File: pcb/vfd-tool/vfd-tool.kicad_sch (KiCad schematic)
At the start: 50 parts, among them J1 Micro_SD_Card, J2 Conn_02x03_Top_Bottom, J3 USB_C_Receptacle_USB2.0, SW1 SW_Push, SW2 SW_Push, U1 RP2040, U2 W25Q32JVSS, U3 TPS562200, Y1 Crystal_GND24

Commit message: Charging circuitry kinda done
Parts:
- added C21, C22: 10uF, Capacitor_SMD:C_0402_1005Metric_Pad0.74x0.62mm_HandSolder, symbol Device:C
- added C23, C26: 0.1uF, Capacitor_SMD:C_0402_1005Metric_Pad0.74x0.62mm_HandSolder, symbol Device:C
- added C24, C25: 22uF, Capacitor_SMD:C_0402_1005Metric_Pad0.74x0.62mm_HandSolder, symbol Device:C
- added C27: 10nF, Capacitor_SMD:C_0402_1005Metric_Pad0.74x0.62mm_HandSolder, symbol Device:C_Small
- added C28: 1uF, Capacitor_SMD:C_0603_1608Metric_Pad1.08x0.95mm_HandSolder, symbol Device:C
- added C29, C30: 4.7uF, Capacitor_SMD:C_0603_1608Metric_Pad1.08x0.95mm_HandSolder, symbol Device:C
- added C31: 0.1uF, Capacitor_SMD:C_0603_1608Metric, symbol Device:C
- added D10, D2: D_Schottky, symbol Device:D_Schottky
- added D3: WS2812B-2020, LED_SMD:LED_WS2812B-2020_PLCC4_2.0x2.0mm, symbol LED:WS2812B-2020
- added D4, D5: LED, LED_SMD:LED_0603_1608Metric, symbol Device:LED
- added D6: PMEG4010CEJ, Diode_SMD:D_SOD-323_HandSoldering, symbol Device:D_Schottky
- added D8, D9: LED, LED_SMD:LED_0603_1608Metric_Pad1.05x0.95mm_HandSolder, symbol Device:LED
- added F1: 500mA, Fuse:Fuse_0402_1005Metric_Pad0.77x0.64mm_HandSolder, symbol Device:Polyfuse
- added J4: Raspberry_Pi_2_3, symbol Connector:Raspberry_Pi_2_3
- added JP1: SolderJumper_2_Open, Connector_PinHeader_1.00mm:PinHeader_1x02_P1.00mm_Vertical, symbol Jumper:SolderJumper_2_Open
- added L2: 2.2uH, Inductor_SMD:L_0805_2012Metric_Pad1.05x1.20mm_HandSolder, symbol Device:L
- added R20, R22: 10k, Resistor_SMD:R_0402_1005Metric_Pad0.72x0.64mm_HandSolder, symbol Device:R
- added R21: 55K, Resistor_SMD:R_0402_1005Metric_Pad0.72x0.64mm_HandSolder, symbol Device:R
- added R23, R24: 1k, Resistor_SMD:R_0603_1608Metric, symbol Device:R
- added R25, R26: 2M, Resistor_SMD:R_0402_1005Metric_Pad0.72x0.64mm_HandSolder, symbol Device:R_Small
- added R27: 10M, Resistor_SMD:R_0402_1005Metric_Pad0.72x0.64mm_HandSolder, symbol Device:R_Small
- added R28: 10K, Resistor_SMD:R_0402_1005Metric_Pad0.72x0.64mm_HandSolder, symbol Device:R
- added R29: 3.9k, Resistor_SMD:R_0402_1005Metric_Pad0.72x0.64mm_HandSolder, symbol Device:R
- added R30, R31: 1K, Resistor_SMD:R_0402_1005Metric_Pad0.72x0.64mm_HandSolder, symbol Device:R
- added R32, R33: 10k, Resistor_SMD:R_0603_1608Metric, symbol Device:R
- added TP1: RPI0_D+, symbol Connector:TestPoint
- added TP2: RPI0_D-, symbol Connector:TestPoint
- added U4: TPS562200, Package_TO_SOT_SMD:SOT-23-6, symbol Regulator_Switching:TPS562200
- added U5: SRV05-4, Package_TO_SOT_SMD:SOT-23-6, symbol Power_Protection:SRV05-4
- added U6: BQ24075RGT, Package_DFN_QFN:VQFN-16-1EP_3x3mm_P0.5mm_EP1.6x1.6mm, symbol Battery_Management:BQ24075RGT
- added U7: MAX17048G_T10, Package_DFN_QFN:DFN-8-1EP_2x2mm_P0.5mm_EP0.6x1.2mm, symbol MAX17048G_T10:MAX17048G_T10
- R18: value 33.2k -> 33K
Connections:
- net 3V3: now also JP1.2 (B), R32.2, R33.2
- net D+_RP2040: now also U5.1 (IO1)
- net D-_RP2040: now also U5.3 (IO2)
- net GND: now also C24.1, C25.1, C26.2, C27.1, C28.2, C29.1, C30.1, C31.2, D3.2 (VSS), J4.14 (GND), J4.20 (GND), J4.25 (GND), J4.30 (GND), J4.34 (GND), J4.39 (GND), J4.6 (GND), J4.9 (GND), R22.2, R23.2, R24.2, R27.2, U5.2 (VN), U6.15 (SYSOFF), U6.17 (VSS), U6.4 (~{CE}), U6.5 (EN2), U6.8 (VSS), U7.1 (CTG), U7.4 (GND), U7.6 (QSTRT), U7.9 (EP)
- net VBUS: now also D6.2 (A), U5.4 (IO3)
- net VSYS: now also C21.2, C22.1, D10.1 (K), R20.1, U4.3 (VIN), U6.6 (EN1)
- net BATT_SDA: now reaches U1.17 (GPIO14)
- net BATT_SDA: now also R32.1, U7.8 (SDA)
- net BATT_SCL: now reaches U1.18 (GPIO15)
- net BATT_SCL: now also R33.1, U7.7 (SCL)
- net MOSI_INTER: now reaches U1.30 (GPIO19)
- net MOSI_INTER: now also J4.38 (GPIO20/MOSI1)
- net MISO_INTER: now reaches U1.31 (GPIO20)
- net MISO_INTER: now also J4.35 (GPIO19/MISO1)
- net RGB_DIN: now reaches U1.32 (GPIO21)
- net RGB_DIN: now also D3.3 (DIN)
- net SCLK_INTER: now reaches U1.34 (GPIO22)
- net SCLK_INTER: now also J4.40 (GPIO21/SCLK1)
- net LED: now reaches U1.35 (GPIO23)
- net LED: now also D5.2 (A)
- net CHRG_CTRL_1: now reaches U1.36 (GPIO24)
- net CHRG_CTRL_1: now also R28.1
- net CHRG_CTRL_2: now reaches U1.37 (GPIO25)
- net CHRG_CTRL_2: now also R29.2
- net BATT_MONITOR: now reaches U1.38 (GPIO26_ADC0)
- net BATT_MONITOR: now also C27.2, R26.2, R27.1
- new net: D4.1 (K), R23.1
- new net: D4.2 (A), JP1.1 (A)
- new net: R21.2, R22.1, U4.4 (VFB)
- new net: C23.1, L2.1, U4.2 (SW)
- new net: C23.2, U4.6 (VBST)
- new net: C21.1, C22.2, U4.1 (GND)
- new net: R20.2, U4.5 (EN)
- new net: D6.1 (K), F1.1
- new net: C28.1, F1.2, U6.13 (IN)
- new net: R28.2, R29.1, U6.16 (ISET)
- new net: D9.1 (K), U6.7 (~{PGOOD})
- new net: D8.1 (K), U6.9 (~{CHG})
- new net: D5.1 (K), R24.1
- new net: D9.2 (A), R31.1
- new net: D8.2 (A), R30.1
- new net: R25.2, R26.1
- new net: J4.1 (3V3), J4.17 (3V3)
- new net: D2.1 (K), J4.2 (5V), J4.4 (5V)
- new net 5V: C24.2, C25.2, C26.1, D2.2 (A), D3.4 (VDD), L2.2, R21.1
- new net B+: C30.2, C31.1, R25.1, U6.2 (BAT), U6.3 (BAT), U7.2 (CELL), U7.3 (VDD)
- new net BAT_TEMP: U6.1 (TS)
- new net GPIO16: U7.5 (~{ALERT})
- new net RGB_DOUT: D3.1 (DOUT)
- new net RPI0_D+: TP1.1
- new net RPI0_D-: TP2.1
- new net VBAT: C29.2, D10.2 (A), R30.2, R31.2, U6.10 (OUT), U6.11 (OUT)
- no-connect marks 2 -> 4
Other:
- note added: "5V"
- note added: "Battery charging"
- note added: "Credit to Zhiayang/mikoto on GitHub"
- note added: "Flash"
- note added: "Fuel gauge"
- note added: "Looooooooooooooooooooooooooooong"
- note added: "Ok max 6A out here"
- note added: "USB"
- note added: "uSD"
- moved on the sheet: C13, C14, C15, C16, C17, C18, C19, C20, D1, J1, J3, L1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

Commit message: USB hub WIP
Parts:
- removed D1: D_Schottky, symbol Device:D_Schottky
- removed J3: USB_C_Receptacle_USB2.0, Connector_USB:USB_C_Receptacle_G-Switch_GT-USB-7010ASV, symbol Connector:USB_C_Receptacle_USB2.0
- removed U5: SRV05-4, Package_TO_SOT_SMD:SOT-23-6, symbol Power_Protection:SRV05-4
- added C34, C35: 30pF, Capacitor_SMD:C_0402_1005Metric_Pad0.74x0.62mm_HandSolder, symbol Device:C
- added D1: LED, LED_SMD:LED_0603_1608Metric, symbol Device:LED
- added D7: D_Schottky, symbol Device:D_Schottky
- added J5: USB_C_Receptacle_USB2.0, Connector_USB:USB_C_Receptacle_G-Switch_GT-USB-7010ASV, symbol Connector:USB_C_Receptacle_USB2.0
- added R34, R35: 5.1K, Resistor_SMD:R_0603_1608Metric, symbol Device:R
- added R36, R39: 10k, symbol Device:R
- added R37: 1K, Resistor_SMD:R_0402_1005Metric_Pad0.72x0.64mm_HandSolder, symbol Device:R
- added R38: 1k, Resistor_SMD:R_0603_1608Metric, symbol Device:R
- added U8: USB2514B_M2, USB2514B_M2:36-SQFN-EXPOSED-PAD, symbol USB2514B_M2:USB2514B_M2
- added U9: SRV05-4, Package_TO_SOT_SMD:SOT-23-6, symbol Power_Protection:SRV05-4
- added Y3: Crystal_GND24, KiCad:SMD3225_4P12288MHZ12PF10PPM4085, symbol Device:Crystal_GND24
- R15, R16: value 5.1K -> 100k; footprint Resistor_SMD:R_0603_1608Metric -> (none)
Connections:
- net CC1: now also J5.A5 (CC1), R34.1; no longer R15.1
- net CC2: now also J5.B5 (CC2), R35.1; no longer R16.1
- net D+_RP2040: now also U8.2 (DP1)
- net D-_RP2040: now also U8.1 (DM1)
- net GND: now also C34.1, C35.1, J5.A1 (GND), J5.A12 (GND), J5.B1 (GND), J5.B12 (GND), J5.S1 (SHIELD), R34.2, R35.2, R36.2, R38.2, R39.2, U8.37 (VSS), U9.2 (VN), Y3.2, Y3.4; no longer R15.2
- net VBUS: now also R15.1, D7.2 (A), J5.A4 (VBUS), J5.A9 (VBUS), J5.B4 (VBUS), J5.B9 (VBUS), U9.4 (IO3)
- net VSYS: now also D7.1 (K)
- net HUB_SDA: now reaches U1.27 (GPIO16)
- net HUB_SDA: now also R36.1, U8.22 (SMBDATA)
- net HUB_SCL: now reaches U1.28 (GPIO17)
- net HUB_SCL: now also R39.1, U8.24 (SMBCLK)
- new net: C34.2, U8.32 (XTAL1), Y3.3
- new net: R15.2, R16.1, U8.27 (VBUS_DET)
- new net: R37.1, U8.33 (XTAL2)
- new net: C35.2, R37.2, Y3.1
- new net: D1.1 (K), R38.1
- new net HUB_RST: U8.26 (~{RESET})
- new net HUB_SUSP: D1.2 (A)
- new net UP_D+: J5.A6 (D+), J5.B6 (D+), U8.31 (DP-UP), U9.1 (IO1)
- new net UP_D-: J5.A7 (D-), J5.B7 (D-), U8.30 (DM-UP), U9.3 (IO2)
- no-connect marks 4 -> 5
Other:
- note added: "Needed or no? Not mentionned by the datasheet"
- note added: "are those I2C?"
- note added: "mm external symbols :joy:"

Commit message: USB hub & PD done
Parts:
- removed R34, R35: 5.1K, Resistor_SMD:R_0603_1608Metric, symbol Device:R
- added C32, C40, C42, C46: 1uF, symbol Device:C
- added C33, C36, C37, C38, C39, C41, C43, C45, C51: 0.1uF, Capacitor_SMD:C_0402_1005Metric_Pad0.74x0.62mm_HandSolder, symbol Device:C
- added C44: 20uF, symbol Device:C
- added C47, C48: 300pF, symbol Device:C
- added C49, C50: 4.7uF, Capacitor_SMD:C_0603_1608Metric, symbol Device:C
- added D11: SP4020, symbol Device:D_TVS_Filled
- added R40: 12k, symbol Device:R
- added R41, R42, R43, R44, R47, R48, R49, R50: 10k, symbol Device:R
- added R45, R46: 100k, symbol Device:R
- added U10: TPS54331DR, Package_SO:SOIC-8_3.9x4.9mm_P1.27mm, symbol TPS54331DR:TPS54331DR
- added U5: FUSB302BMPX, Package_DFN_QFN:WQFN-14-1EP_2.5x2.5mm_P0.5mm_EP1.45x1.45mm, symbol Interface_USB:FUSB302BMPX
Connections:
- net 3V3: now also R36.2, R39.2, U8.10 (VDDA33-2), U8.15 (VDD33IO), U8.23 (VDD33REG), U8.29 (VDDA33-3), U8.36 (VDDPLLREF), U8.5 (VDDA33-1), C32.1, C33.1, C36.1, C37.1, C38.1, C45.1, C46.1, R41.2, R42.2, R43.2, R44.2, R46.2, R48.1, R49.1, R50.1, U5.3 (VDD), U5.4 (VDD)
- net CC1: now also C47.1, U5.10 (CC1), U5.11 (CC1)
- net CC2: now also C48.1, U5.1 (CC2), U5.14 (CC2)
- net GND: now also C32.2, C33.2, C36.2, C37.2, C38.2, C39.2, C40.2, C41.2, C42.2, C43.2, C44.2, C45.2, C46.2, C47.2, C48.2, C49.2, C50.2, C51.2, D11.1 (A1), R40.2, R45.2, R47.2, U5.15 (GND), U5.8 (GND), U5.9 (GND); no longer R36.2, R39.2
- net HUB_RST: now also R46.1
- net HUB_SUSP: now also U8.28 (SUSP_IND), R45.1
- net RPI0_D+: now also U8.4 (DP2)
- net RPI0_D-: now also U8.3 (DM2)
- net VBUS: now also C49.1, C50.1, C51.1, D11.2 (A2), U5.2 (VBUS); no longer U9.4 (IO3)
- net at U8.13 (OCS1): now also R44.1
- net at U8.14 (CRFILT): now also C39.1, C40.1
- net at U8.17 (OCS2): now also R43.1
- net at U8.19 (OCS3): now also R42.1
- net at U8.21 (OCS4): now also R41.1
- net at U8.25 (CFG_SEL1): now also R47.1
- net at U8.34 (PLLFILT): now also C41.1, C42.1
- net at U8.35 (RBIAS): now also R40.1
- net EXTRA_USB4_D-: now reaches U8.6 (DM3)
- net EXTRA_USB4_D-: now also U8.8 (DM4)
- net EXTRA_USB3_D+: now reaches U8.7 (DP3)
- net EXTRA_USB4_D+: now reaches U8.9 (DP4)
- net PD_SDA: now reaches U1.11 (GPIO8)
- net PD_SDA: now also R48.2, U5.7 (SDA)
- net PD_SCL: now reaches U1.12 (GPIO9)
- net PD_SCL: now also R49.2, U5.6 (SCL)
- net PD_INT: now reaches U1.8 (GPIO6)
- net PD_INT: now also R50.2, U5.5 (INT_N)
- net D+_RP2040 renamed RP2040_D+
- net D-_RP2040 renamed RP2040_D-
- new net VCONN: C43.1, C44.1, U5.12 (VCONN), U5.13 (VCONN)
- no-connect marks 5 -> 9
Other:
- note added: "1 0 = SMBus"
- note added: "Conn"
- note added: "DNP?"
- note added: "NON_REM0"
- note added: "NON_REM1"
- note added: "PD"
- note added: "We bypass the inefficient regs on batts"
- note removed: "Needed or no? Not mentionned by the datasheet"
- note removed: "are those I2C?"
- moved on the sheet: C16, C17, C18, C19, C20, C21, C22, C23, C24, C25, C27, C28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

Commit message: Added switching regulator for VBUS (+20V), Board to board connector
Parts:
- added C52: 0.1uF, Capacitor_SMD:C_0402_1005Metric_Pad0.74x0.62mm_HandSolder, symbol Device:C
- added C53: 0.01uF, Capacitor_SMD:C_0402_1005Metric_Pad0.74x0.62mm_HandSolder, symbol Device:C
- added C54: 39pF, Capacitor_SMD:C_0402_1005Metric_Pad0.74x0.62mm_HandSolder, symbol Device:C
- added C55, C57: 33uF, Capacitor_SMD:C_0402_1005Metric_Pad0.74x0.62mm_HandSolder, symbol Device:C
- added C56: 4.7nF, Capacitor_SMD:C_0402_1005Metric_Pad0.74x0.62mm_HandSolder, symbol Device:C
- added D12, D13, D14: D_Schottky, symbol Device:D_Schottky
- added J3, J6: Conn_02x15_Odd_Even, symbol Connector_Generic:Conn_02x15_Odd_Even
- added L3: 6.8uH, symbol Device:L
- added R34: 332K, symbol Device:R
- added R35: 82k, symbol Device:R
- added R51, R53: 1.9k, symbol Device:R
- added R52: 10k, symbol Device:R
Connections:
- net 3V3: now also J3.15 (Pin_15), J3.17 (Pin_17)
- net 5V: now also J3.19 (Pin_19), J3.21 (Pin_21)
- net EXTRA_USB3_D+: now also J3.24 (Pin_24)
- net EXTRA_USB4_D+: now also J3.16 (Pin_16)
- net EXTRA_USB4_D-: now also J3.18 (Pin_18), J3.26 (Pin_26)
- net GND: now also D7.1 (K), U10.7 (GND), C53.2, C54.2, C55.2, C57.2, J3.13 (Pin_13), J3.14 (Pin_14), J3.20 (Pin_20), J3.22 (Pin_22), J3.28 (Pin_28), J3.30 (Pin_30), J3.5 (Pin_5), J3.6 (Pin_6), J6.5 (Pin_5), J6.6 (Pin_6), R35.2, R51.2, R53.2
- net MISO_INTER: now also J4.21 (MISO0/GPIO9), J6.1 (Pin_1); no longer J4.35 (GPIO19/MISO1)
- net MOSI_INTER: now also J4.19 (MOSI0/GPIO10), J6.3 (Pin_3); no longer J4.38 (GPIO20/MOSI1)
- net RGB_DOUT: now also J6.2 (Pin_2)
- net SCLK_INTER: now also J4.23 (SCLK0/GPIO11), J6.4 (Pin_4); no longer J4.40 (GPIO21/SCLK1)
- net VBUS: now also D13.2 (A), J3.10 (Pin_10), J3.11 (Pin_11), J3.12 (Pin_12), J3.7 (Pin_7), J3.8 (Pin_8), J3.9 (Pin_9); no longer C49.1, C50.1, C51.1, D7.2 (A)
- net VCONN: now also J3.23 (Pin_23), J3.25 (Pin_25), J3.27 (Pin_27), J3.29 (Pin_29)
- net VSYS: now also D12.1 (K); no longer D7.1 (K)
- net at U10.1 (BOOT): now also C52.2
- net EXT_PWR: now reaches U10.2 (VIN)
- net EXT_PWR: now also C49.1, C50.1, C51.1, D13.1 (K), D14.1 (K), R34.1
- net at U10.3 (EN): now also R34.2, R35.1
- net at U10.4 (SS): now also C53.1
- net at U10.5 (VSENSE): now also R52.2, R53.1
- net at U10.6 (COMP): now also C54.1, C56.1
- net at U10.8 (PH): now also D7.2 (A), C52.1, L3.1
- net RP2040_GPIO10: now reaches U1.13 (GPIO10)
- net RP2040_GPIO11: now reaches U1.14 (GPIO11)
- net RP2040_GPIO12: now reaches U1.15 (GPIO12)
- net RP2040_GPIO13: now reaches U1.16 (GPIO13)
- net RP2040_GPIO18: now reaches U1.29 (GPIO18)
- net GPIO7: now reaches U1.9 (GPIO7)
- net RP2040_CE: now reaches J4.24 (~{CE0}/GPIO8)
- new net: D14.2 (A), J3.1 (Pin_1), J3.2 (Pin_2), J3.3 (Pin_3), J3.4 (Pin_4)
- new net: C55.1, C57.1, D12.2 (A), L3.2, R52.1
- new net: C56.2, R51.1
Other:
- note added: "Redundant?"
- note added: "Redundant? VBAT outputs at 5.5V @ 6A -> change fuse to BAT"
- note added: "TODO: 1. Optimize power topology 2. Fix calculated values 3. add a step-up incase the EXT_PWR is below 5V"
- note removed: "TODO: 1. Multiple power inputs/priority 2. Battery charging"
- moved on the sheet: C27, C28, C29, C30, C31, C43, C44, C45, C46, C47, C48, D10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

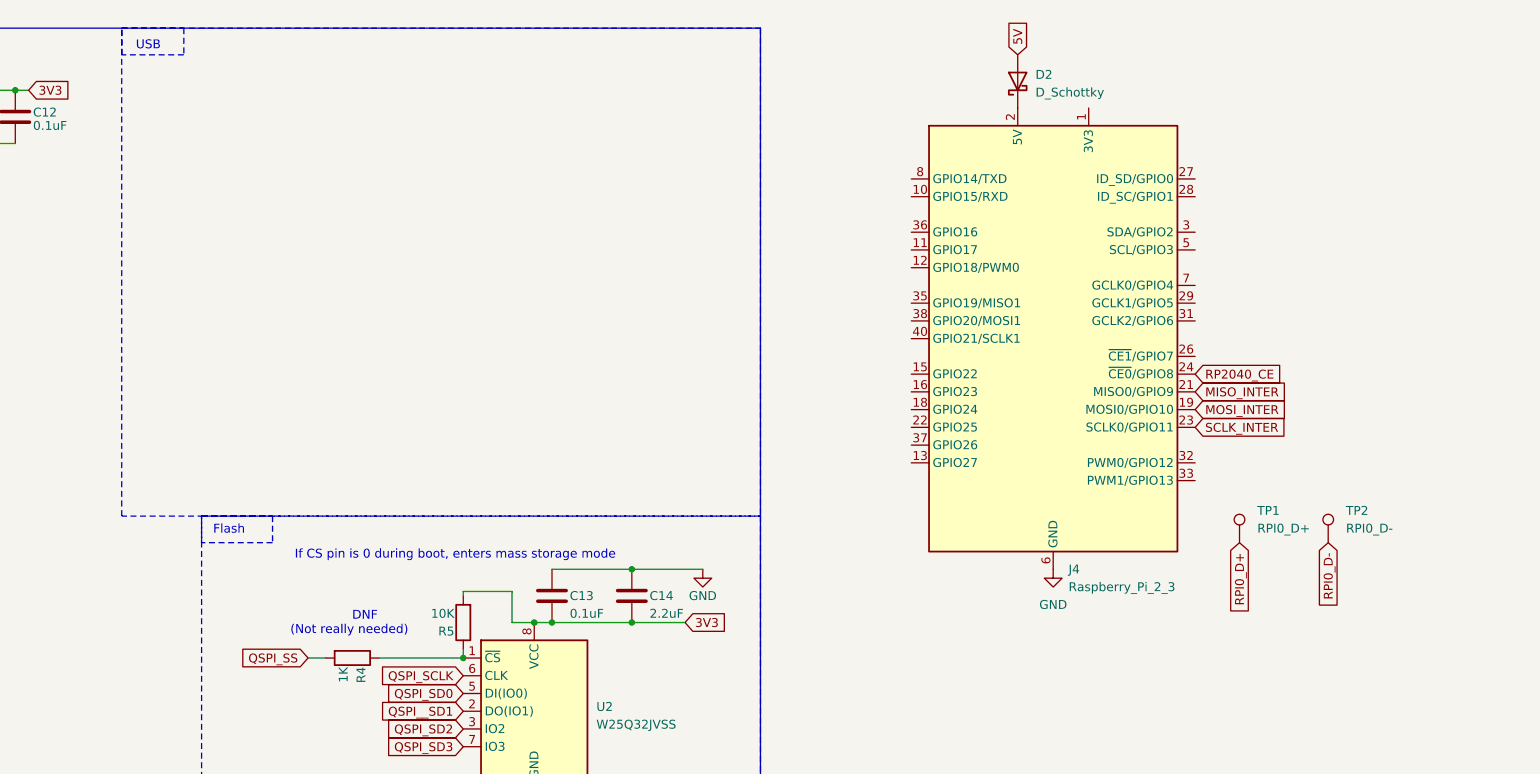
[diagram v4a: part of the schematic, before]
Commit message: added RTC
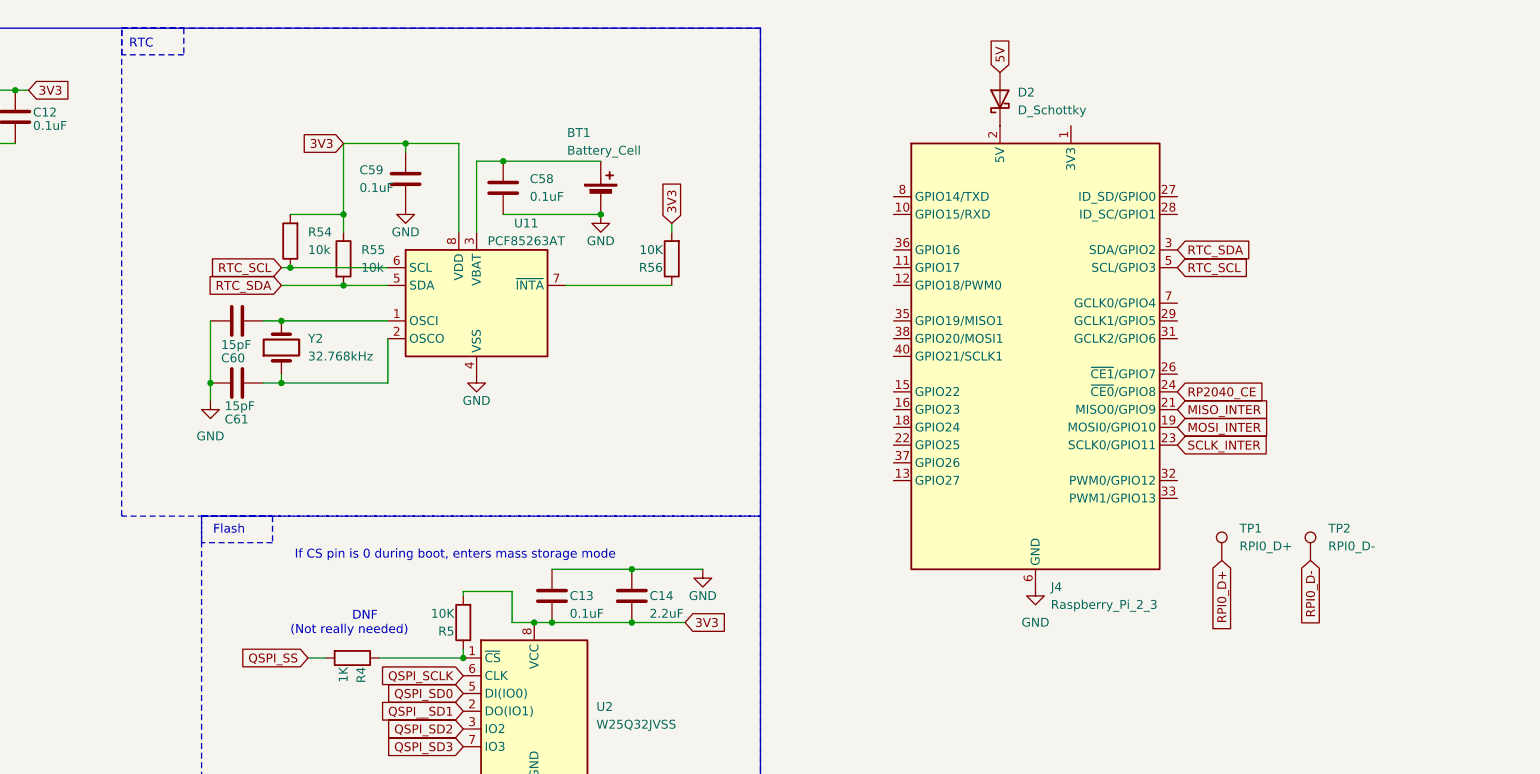
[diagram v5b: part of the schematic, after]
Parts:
- added BT1: Battery_Cell, symbol Device:Battery_Cell
- added C58, C59: 0.1uF, symbol Device:C
- added C60, C61: 15pF, Capacitor_SMD:C_0402_1005Metric_Pad0.74x0.62mm_HandSolder, symbol Device:C
- added R54, R55: 10k, Resistor_SMD:R_0402_1005Metric_Pad0.72x0.64mm_HandSolder, symbol Device:R
- added R56: 10K, Resistor_SMD:R_0402_1005Metric_Pad0.72x0.64mm_HandSolder, symbol Device:R
- added U11: PCF85263AT, Package_SO:SOIC-8_3.9x4.9mm_P1.27mm, symbol Timer_RTC:PCF85263AT
- added Y2: 32.768kHz, symbol Device:Crystal
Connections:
- net 3V3: now also C59.1, R54.2, R55.1, R56.2, U11.8 (VDD)
- net GND: now also BT1.2 (-), C58.2, C59.2, C60.2, C61.2, U11.4 (VSS)
- net RTC_SDA: now reaches J4.3 (SDA/GPIO2)
- net RTC_SDA: now also R55.2, U11.5 (SDA)
- net RTC_SCL: now reaches J4.5 (SCL/GPIO3)
- net RTC_SCL: now also R54.1, U11.6 (SCL)
- new net: BT1.1 (+), C58.1, U11.3 (VBAT)
- new net: C60.1, U11.1 (OSCI), Y2.2
- new net: C61.1, U11.2 (OSCO), Y2.1
- new net: R56.1, U11.7 (~{INTA})
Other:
- note added: "RTC"
- moved on the sheet: D2, J4, TP1, TP2
